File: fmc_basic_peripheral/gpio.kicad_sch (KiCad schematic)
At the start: 43 parts, among them J6 PM2.54-2x6, SW1 DSHP04TSGET, SW10 TL3342F160QG, SW2 TL3342F160QG, SW8 TL3342F160QG, SW9 TL3342F160QG, U14 TXS02612RTWR

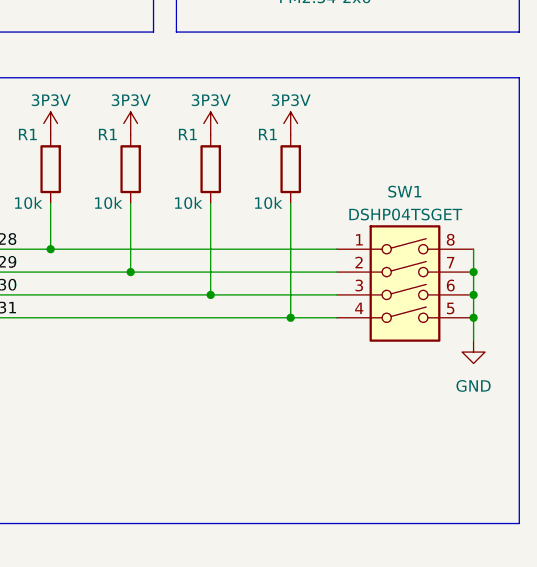
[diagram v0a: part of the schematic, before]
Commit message: fmc_basic_peripheral: rotate SW1, bump to 1.0.6
Signed-off-by: Huang Rui <vowstar@gmail.com>
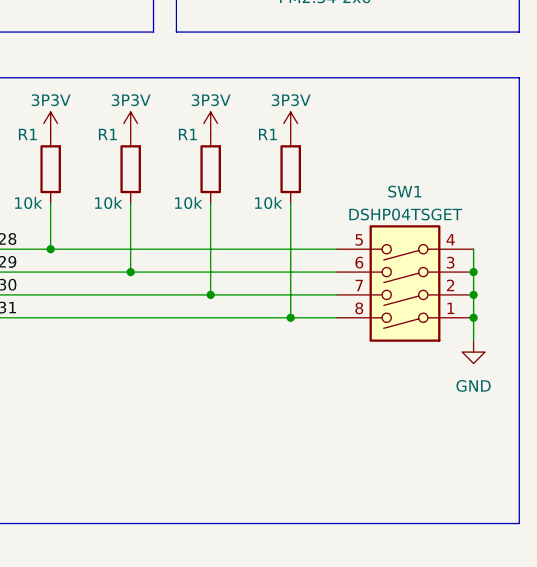
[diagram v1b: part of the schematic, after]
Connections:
- net GND: now also SW1.1, SW1.2, SW1.3, SW1.4; no longer SW1.5, SW1.6, SW1.7, SW1.8
- net HVGPIO28: now also SW1.5; no longer SW1.1
- net HVGPIO29: now also SW1.6; no longer SW1.2
- net HVGPIO30: now also SW1.7; no longer SW1.3
- net HVGPIO31: now also SW1.8; no longer SW1.4
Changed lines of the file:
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@@
   (title_block
     (title "GPIO")
-    (date "2023-03-02")
-    (rev "1.0.5")
+    (date "2023-05-09")
+    (rev "1.0.6")
     (company "CHIPS Alliance")
     (comment 1 "Rui Huang (2023-03-02)")
     (comment 2 "Rui Huang (2023-03-02)")
-    (comment 4 "Rui Huang (2023-03-02)")
+    (comment 4 "Rui Huang (2023-05-09)")
   )
   (junction (at 246.38 125.73) (diameter 0) (color 0 0 0 0)
@@
   (junction (at 187.96 128.27) (diameter 0) (color 0 0 0 0)
   )
+  (junction (at 275.59 128.27) (diameter 0) (color 0 0 0 0)
+  )
   (junction (at 175.26 38.1) (diameter 0) (color 0 0 0 0)
   )
+  (junction (at 275.59 123.19) (diameter 0) (color 0 0 0 0)
+  )
   (junction (at 49.53 38.1) (diameter 0) (color 0 0 0 0)
   )
@@
   (junction (at 179.07 125.73) (diameter 0) (color 0 0 0 0)
   )
+  (junction (at 275.59 125.73) (diameter 0) (color 0 0 0 0)
+  )
   (junction (at 111.76 38.1) (diameter 0) (color 0 0 0 0)
   )
@@
   (junction (at 152.4 71.12) (diameter 0) (color 0 0 0 0)
   )
-  (junction (at 275.59 125.73) (diameter 0) (color 0 0 0 0)
-  )
   (junction (at 107.95 153.67) (diameter 0) (color 0 0 0 0)
   )
   (junction (at 255.27 128.27) (diameter 0) (color 0 0 0 0)
   )
-  (junction (at 275.59 128.27) (diameter 0) (color 0 0 0 0)
-  )
   (junction (at 228.6 120.65) (diameter 0) (color 0 0 0 0)
   )
@@
   (junction (at 113.03 101.6) (diameter 0) (color 0 0 0 0)
   )
-  (junction (at 275.59 123.19) (diameter 0) (color 0 0 0 0)
-  )
   (junction (at 237.49 60.96) (diameter 0) (color 0 0 0 0)
   )
@@
     (stroke (width 0) (type default))
   )
-  (wire (pts (xy 275.59 120.65) (xy 275.59 123.19))
-    (stroke (width 0) (type default))
-  )
   (wire (pts (xy 81.28 50.8) (xy 91.44 50.8))
     (stroke (width 0) (type default))
@@
     (stroke (width 0) (type default))
   )
+  (wire (pts (xy 275.59 125.73) (xy 275.59 128.27))
+    (stroke (width 0) (type default))
+  )
   (wire (pts (xy 185.42 50.8) (xy 195.58 50.8))
     (stroke (width 0) (type default))
@@
     (stroke (width 0) (type default))
   )
-  (wire (pts (xy 275.59 125.73) (xy 275.59 128.27))
-    (stroke (width 0) (type default))
-  )
   (bus (pts (xy 80.01 121.92) (xy 80.01 124.46))
     (stroke (width 0) (type default))
@@
     (stroke (width 0) (type default))
   )
-  (wire (pts (xy 275.59 128.27) (xy 275.59 130.81))
-    (stroke (width 0) (type default))
-  )
   (wire (pts (xy 274.32 55.88) (xy 265.43 55.88))
     (stroke (width 0) (type default))
@@
     (stroke (width 0) (type default))
   )
+  (wire (pts (xy 275.59 120.65) (xy 275.59 123.19))
+    (stroke (width 0) (type default))
+  )
   (wire (pts (xy 49.53 38.1) (xy 52.07 38.1))
     (stroke (width 0) (type default))
@@
     (stroke (width 0) (type default))
   )
+  (wire (pts (xy 275.59 128.27) (xy 275.59 130.81))
+    (stroke (width 0) (type default))
+  )
   (wire (pts (xy 90.17 153.67) (xy 107.95 153.67))
     (stroke (width 0) (type default))
@@
     (stroke (width 0) (type default))
   )
+  (wire (pts (xy 275.59 123.19) (xy 275.59 125.73))
+    (stroke (width 0) (type default))
+  )
   (wire (pts (xy 243.84 55.88) (xy 252.73 55.88))
     (stroke (width 0) (type default))
@@
     (stroke (width 0) (type default))
   )
-  (wire (pts (xy 275.59 123.19) (xy 275.59 125.73))
-    (stroke (width 0) (type default))
-  )
   (wire (pts (xy 82.55 119.38) (xy 92.71 119.38))
     (stroke (width 0) (type default))
@@
     )
   )
-  (symbol (lib_id "Switch:SW_DIP_x04") (at 267.97 125.73 0) (unit 1)
-    (in_bom yes) (on_board yes) (dnp no) (fields_autoplaced)
-    (property "Reference" "SW1" (at 267.97 114.3 0)
-      (effects (font (size 1.27 1.27)))
-    )
-    (property "Value" "DSHP04TSGET" (at 267.97 116.84 0)
-      (effects (font (size 1.27 1.27)))
-    )
-    (property "Footprint" "Button_Switch_SMD:SW_DIP_SPSTx04_Slide_KingTek_DSHP04TS_W7.62mm_P1.27mm" (at 267.97 125.73 0)
-      (effects (font (size 1.27 1.27)) hide)
-    )
-    (property "Datasheet" "https://atta.szlcsc.com/upload/public/pdf/source/20150928/1457707425288.pdf" (at 267.97 125.73 0)
-      (effects (font (size 1.27 1.27)) hide)
-    )
-    (pin "1")
-    (pin "2")
-    (pin "3")
-    (pin "4")
-    (pin "5")
-    (pin "6")
-    (pin "7")
-    (pin "8")
-    (instances
-      (project "fmc_usb_gpio_spi_jtag"
-        (path "/387bfcf1-ae49-4b85-be89-3bb02ce2e960/9cd800a1-5b4a-4dab-b708-f8f78f4f7813"
-          (reference "SW1") (unit 1)
-        )
-        (path "/387bfcf1-ae49-4b85-be89-3bb02ce2e960/8f11314c-d9eb-415d-8d76-07f3be42979a"
-          (reference "SW1") (unit 1)
-        )
-      )
-    )
-  )
   (symbol (lib_id "CHIPSAlliance_Power:3P3V") (at 132.08 82.55 0) (unit 1)
     (in_bom yes) (on_board yes) (dnp no)
@@
         )
       )
+    )
+  )
+  (symbol (lib_id "Switch:SW_DIP_x04") (at 267.97 123.19 180) (unit 1)
+    (in_bom yes) (on_board yes) (dnp no) (fields_autoplaced)
+    (property "Reference" "SW1" (at 267.97 114.3 0)
+      (effects (font (size 1.27 1.27)))
+    )
+    (property "Value" "DSHP04TSGET" (at 267.97 116.84 0)
+      (effects (font (size 1.27 1.27)))
+    )
+    (property "Footprint" "Button_Switch_SMD:SW_DIP_SPSTx04_Slide_KingTek_DSHP04TS_W7.62mm_P1.27mm" (at 267.97 123.19 0)
+      (effects (font (size 1.27 1.27)) hide)
+    )
+    (property "Datasheet" "https://atta.szlcsc.com/upload/public/pdf/source/20150928/1457707425288.pdf" (at 267.97 123.19 0)
+      (effects (font (size 1.27 1.27)) hide)
+    )
+    (pin "1")
+    (pin "2")
+    (pin "3")
+    (pin "4")
+    (pin "5")
+    (pin "6")
+    (pin "7")
+    (pin "8")
+    (instances
+      (project "fmc_usb_gpio_spi_jtag"
+        (path "/387bfcf1-ae49-4b85-be89-3bb02ce2e960/9cd800a1-5b4a-4dab-b708-f8f78f4f7813"
+          (reference "SW1") (unit 1)
+        )
+        (path "/387bfcf1-ae49-4b85-be89-3bb02ce2e960/8f11314c-d9eb-415d-8d76-07f3be42979a"
+          (reference "SW1") (unit 1)
+        )
+      )

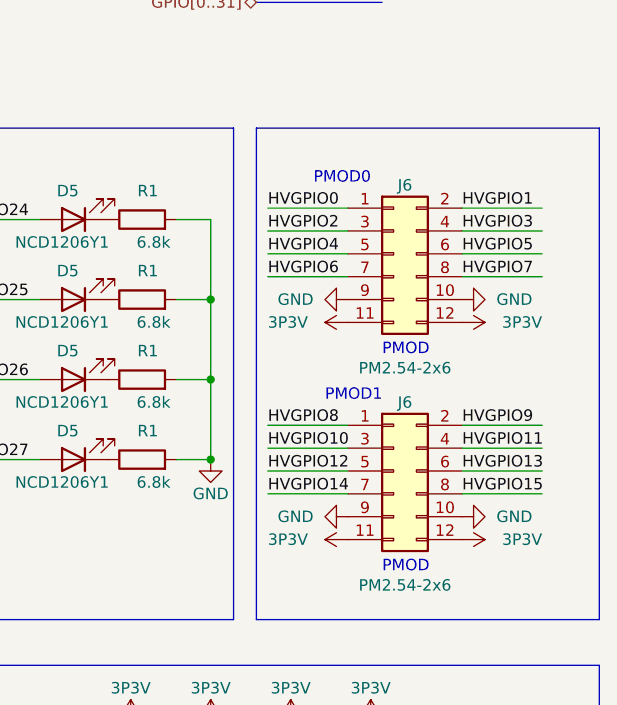
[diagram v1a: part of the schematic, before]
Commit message: fmc_basic_peripheral: fix GPIO PMOD schematic
- Fix PMOD symbol pin order
- Followed Digilent Pmod Interface Specification 1.2.0

Signed-off-by: Huang Rui <vowstar@gmail.com>
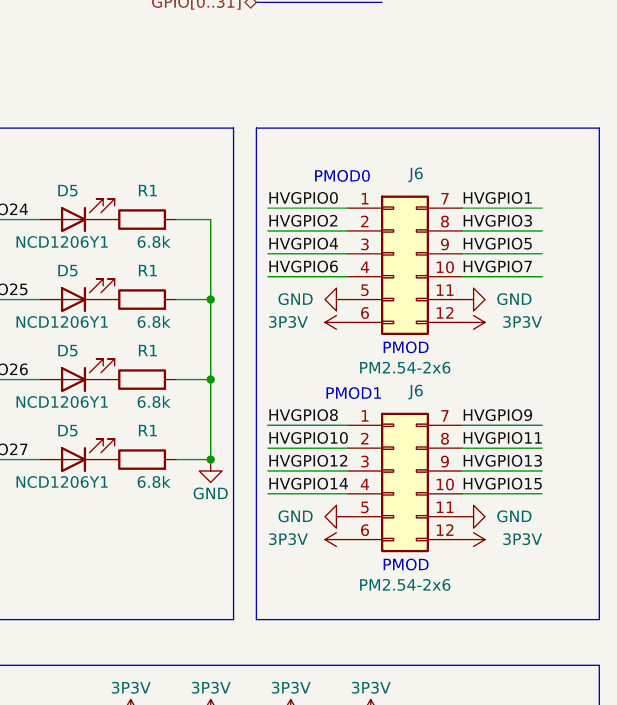
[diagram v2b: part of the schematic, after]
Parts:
- J6: symbol Connector_Generic:Conn_02x06_Odd_Even -> CHIPSAlliance_Connector:Conn_PMOD_12
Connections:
- net 3P3V: now also J6.6 (Pin_6), J6.6 (Pin_6); no longer J6.11 (Pin_11), J6.11 (Pin_11)
- net GND: now also J6.11 (Pin_11), J6.11 (Pin_11), J6.5 (Pin_5), J6.5 (Pin_5); no longer J6.10 (Pin_10), J6.10 (Pin_10), J6.9 (Pin_9), J6.9 (Pin_9)
- net HVGPIO1: now also J6.7 (Pin_7); no longer J6.2 (Pin_2)
- net HVGPIO10: now also J6.2 (Pin_2); no longer J6.3 (Pin_3)
- net HVGPIO11: now also J6.8 (Pin_8); no longer J6.4 (Pin_4)
- net HVGPIO12: now also J6.3 (Pin_3); no longer J6.5 (Pin_5)
- net HVGPIO13: now also J6.9 (Pin_9); no longer J6.6 (Pin_6)
- net HVGPIO14: now also J6.4 (Pin_4); no longer J6.7 (Pin_7)
- net HVGPIO15: now also J6.10 (Pin_10); no longer J6.8 (Pin_8)
- net HVGPIO2: now also J6.2 (Pin_2); no longer J6.3 (Pin_3)
- net HVGPIO3: now also J6.8 (Pin_8); no longer J6.4 (Pin_4)
- net HVGPIO4: now also J6.3 (Pin_3); no longer J6.5 (Pin_5)
- net HVGPIO5: now also J6.9 (Pin_9); no longer J6.6 (Pin_6)
- net HVGPIO6: now also J6.4 (Pin_4); no longer J6.7 (Pin_7)
- net HVGPIO7: now also J6.10 (Pin_10); no longer J6.8 (Pin_8)
- net HVGPIO9: now also J6.7 (Pin_7); no longer J6.2 (Pin_2)
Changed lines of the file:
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@@
     (comment 1 "Rui Huang (2023-03-02)")
     (comment 2 "Rui Huang (2023-03-02)")
-    (comment 4 "Rui Huang (2023-05-09)")
+    (comment 4 "Rui Huang (2023-12-07)")
   )
   (junction (at 246.38 125.73) (diameter 0) (color 0 0 0 0)
@@
     )
   )
-  (symbol (lib_id "Connector_Generic:Conn_02x06_Odd_Even") (at 257.81 55.88 0) (unit 1)
-    (in_bom yes) (on_board yes) (dnp no)
-    (property "Reference" "J6" (at 259.08 48.26 0)
+  (symbol (lib_id "CHIPSAlliance_Connector:Conn_PMOD_12") (at 256.54 49.53 0) (unit 1)
+    (in_bom yes) (on_board yes) (dnp no)
+    (property "Reference" "J6" (at 260.35 46.99 0)
       (effects (font (size 1.27 1.27)))
     )
@@
       (effects (font (size 1.27 1.27)))
     )
-    (property "Footprint" "Connector_PinSocket_2.54mm:PinSocket_2x06_P2.54mm_Vertical" (at 257.81 55.88 0)
-      (effects (font (size 1.27 1.27)) hide)
-    )
-    (property "Datasheet" "https://atta.szlcsc.com/upload/public/pdf/source/20220729/B685A447B6E7D9EA1A3EF6B07540DD20.pdf" (at 257.81 55.88 0)
+    (property "Footprint" "Connector_PinSocket_2.54mm:PinSocket_2x06_P2.54mm_Vertical" (at 256.54 49.53 0)
+      (effects (font (size 1.27 1.27)) hide)
+    )
+    (property "Datasheet" "https://atta.szlcsc.com/upload/public/pdf/source/20220729/B685A447B6E7D9EA1A3EF6B07540DD20.pdf" (at 256.54 49.53 0)
       (effects (font (size 1.27 1.27)) hide)
     )
@@
     )
   )
-  (symbol (lib_id "Connector_Generic:Conn_02x06_Odd_Even") (at 257.81 80.01 0) (unit 1)
-    (in_bom yes) (on_board yes) (dnp no)
-    (property "Reference" "J6" (at 259.08 72.39 0)
+  (symbol (lib_id "CHIPSAlliance_Connector:Conn_PMOD_12") (at 256.54 73.66 0) (unit 1)
+    (in_bom yes) (on_board yes) (dnp no)
+    (property "Reference" "J6" (at 260.35 71.12 0)
       (effects (font (size 1.27 1.27)))
     )
@@
       (effects (font (size 1.27 1.27)))
     )
-    (property "Footprint" "Connector_PinSocket_2.54mm:PinSocket_2x06_P2.54mm_Vertical" (at 257.81 80.01 0)
-      (effects (font (size 1.27 1.27)) hide)
-    )
-    (property "Datasheet" "https://atta.szlcsc.com/upload/public/pdf/source/20220729/B685A447B6E7D9EA1A3EF6B07540DD20.pdf" (at 257.81 80.01 0)
-      (effects (font (size 1.27 1.27)) hide)
-    )
+    (property "Footprint" "Connector_PinSocket_2.54mm:PinSocket_2x06_P2.54mm_Vertical" (at 256.54 73.66 0)
+      (effects (font (size 1.27 1.27)) hide)
+    )
+    (property "Datasheet" "https://atta.szlcsc.com/upload/public/pdf/source/20220729/B685A447B6E7D9EA1A3EF6B07540DD20.pdf" (at 256.54 73.66 0)
+      (effects (font (size 1.27 1.27)) hide)
+    )
